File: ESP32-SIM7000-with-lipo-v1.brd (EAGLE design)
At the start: 90 x 60 mm, 65 parts, among them IC2 TXB0104, Q1 BSS138L, Q2 BSS138L, Q3 9013, Q5 9013, U3 ESP-WROOM-32, U4 MCP73831T-2ACI/OT, X1 LTE-uFL

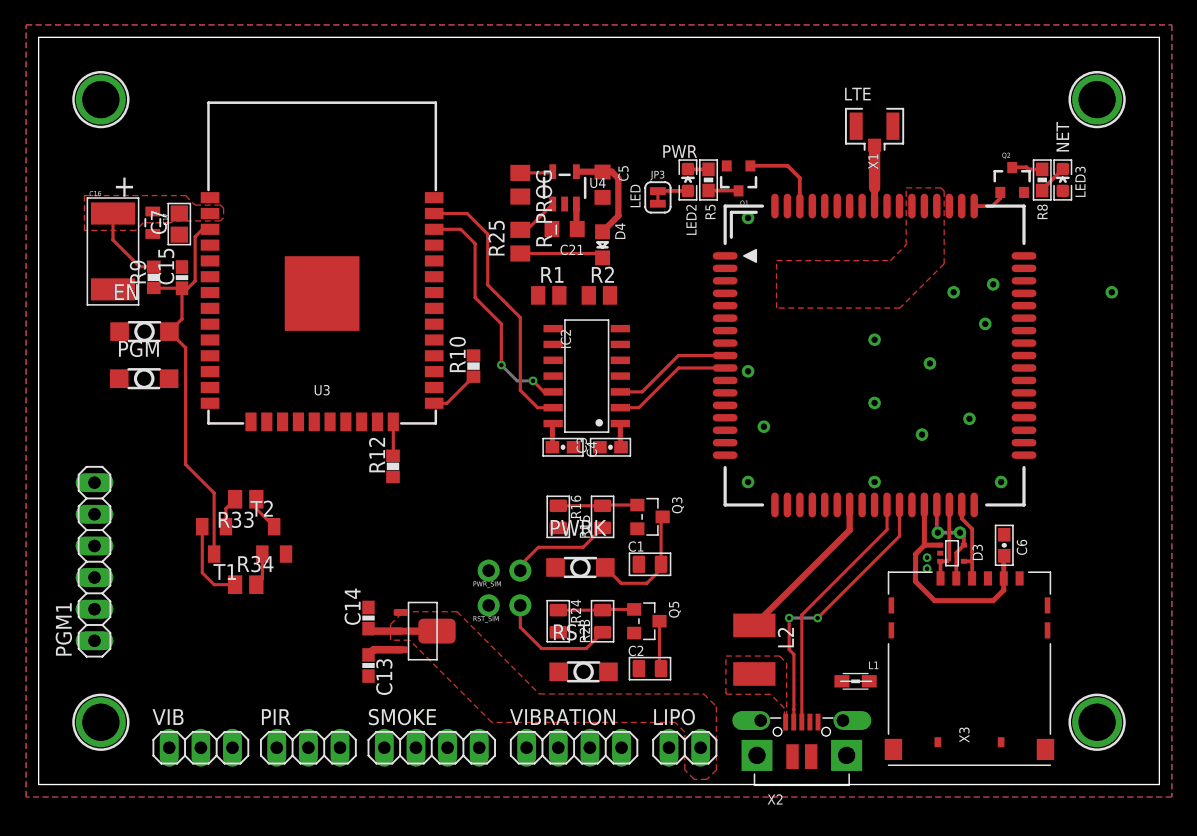
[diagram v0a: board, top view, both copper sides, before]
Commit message: route remaining traces
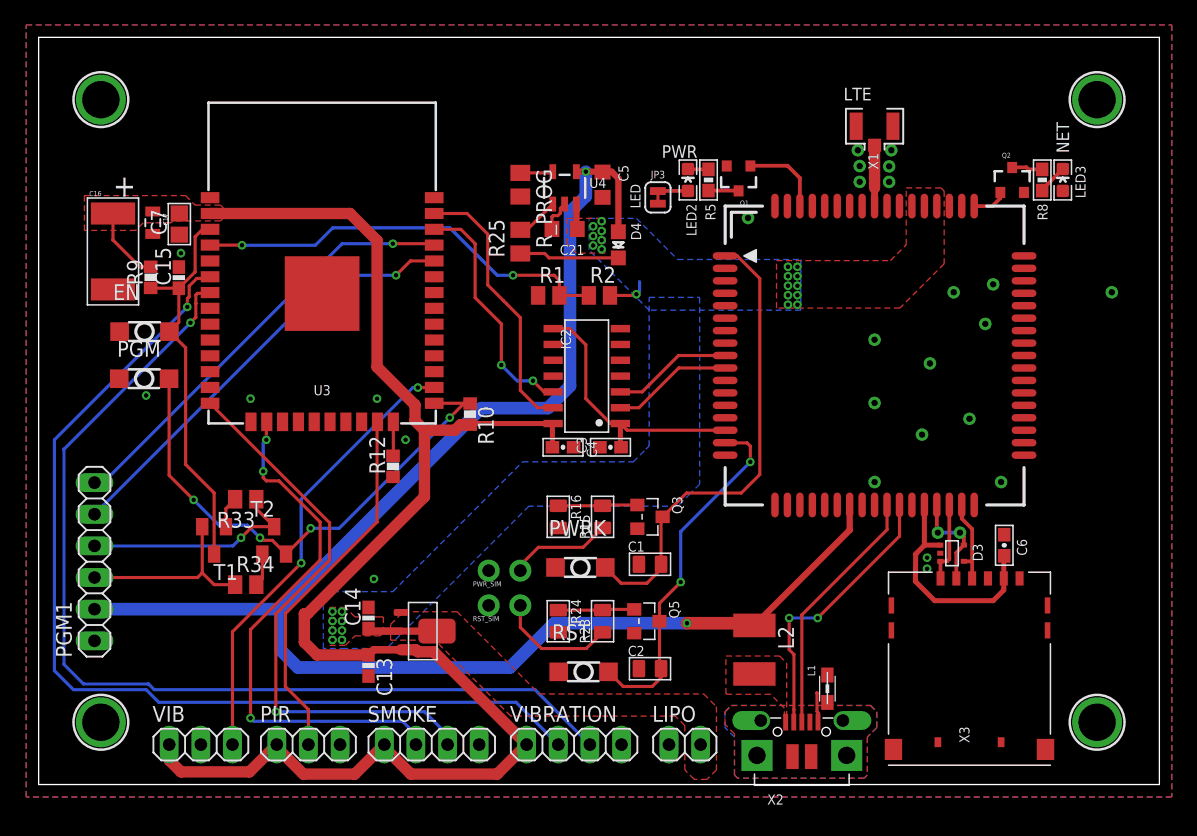
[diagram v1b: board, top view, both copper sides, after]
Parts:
- moved R10 3.86 mm to (34.6, 29.7), turned to 270 degrees
- moved L1 2.34 mm to (63.3, 7.69), turned to 270 degrees
- moved D4 1.27 mm to (46.6, 43.3)
- moved LIPO 0.25 mm to (51.9, 3.21)
- moved PIR 0.25 mm to (21.7, 3.21)
- moved SMOKE 0.25 mm to (31.6, 3.21)
- moved VIB 0.25 mm to (13.0, 3.21)
- moved VIBRATION 0.25 mm to (43.0, 3.21)
- moved C15 0.25 mm to (11.3, 40.7)
- moved R9 0.25 mm to (9.00, 40.7)
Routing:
- net +3V3: track 11.0 -> 127.9 mm
- net VBUS: track 21.3 -> 127.6 mm, vias 0 -> 2
- net VIB_SDA: track 0.00 -> 80.3 mm, vias 0 -> 1
- net VIB_SCL: track 0.00 -> 80.3 mm, vias 0 -> 1
- net SMOKE_SCL: track 0.00 -> 45.9 mm, vias 0 -> 1
- net SMOKE_SDA: track 0.00 -> 43.3 mm, vias 0 -> 3
- net IO0: track 4.04 -> 42.0 mm, vias 0 -> 4
- net VIBRATION: track 0.00 -> 36.4 mm, vias 0 -> 2
- net RXD0: track 0.00 -> 35.7 mm, vias 0 -> 1
- net TXD0: track 0.00 -> 35.3 mm, vias 0 -> 1
- net BAT_LEVEL: track 0.00 -> 33.9 mm, vias 0 -> 2
- net PIR: track 0.00 -> 29.8 mm
- net PWRKEY: track 9.72 -> 38.2 mm
- net SIM_RESET: track 3.86 -> 28.8 mm, vias 0 -> 2
- net 1.8V: track 1.93 -> 21.7 mm
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- added copper zone on layer 16, net +4.1V
- added copper zone on layer 1, net SHIELD
- added copper zone on layer 16, net SHIELD
- removed copper zone on layer 1, net N$3

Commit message: Naming components
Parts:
- renumbered PGM1 to PROGRAM

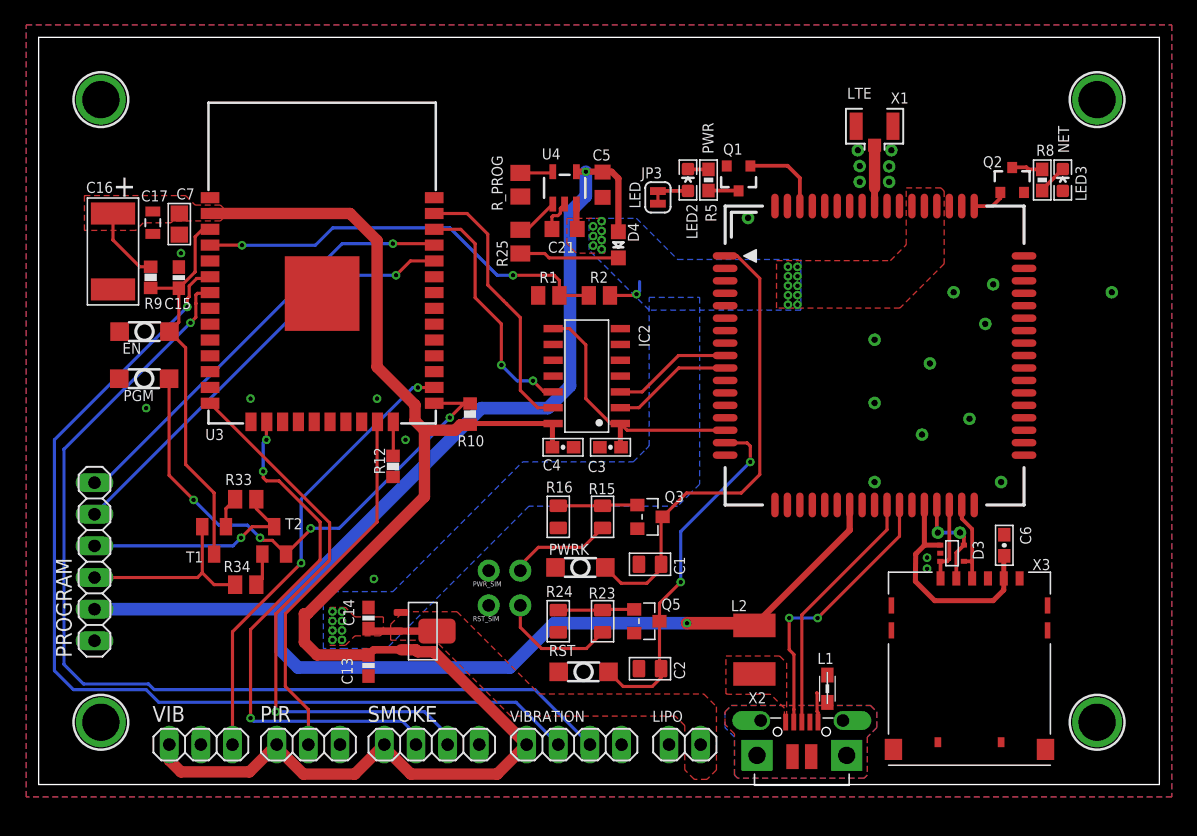
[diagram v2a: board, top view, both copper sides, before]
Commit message: adds vias and completes DRC
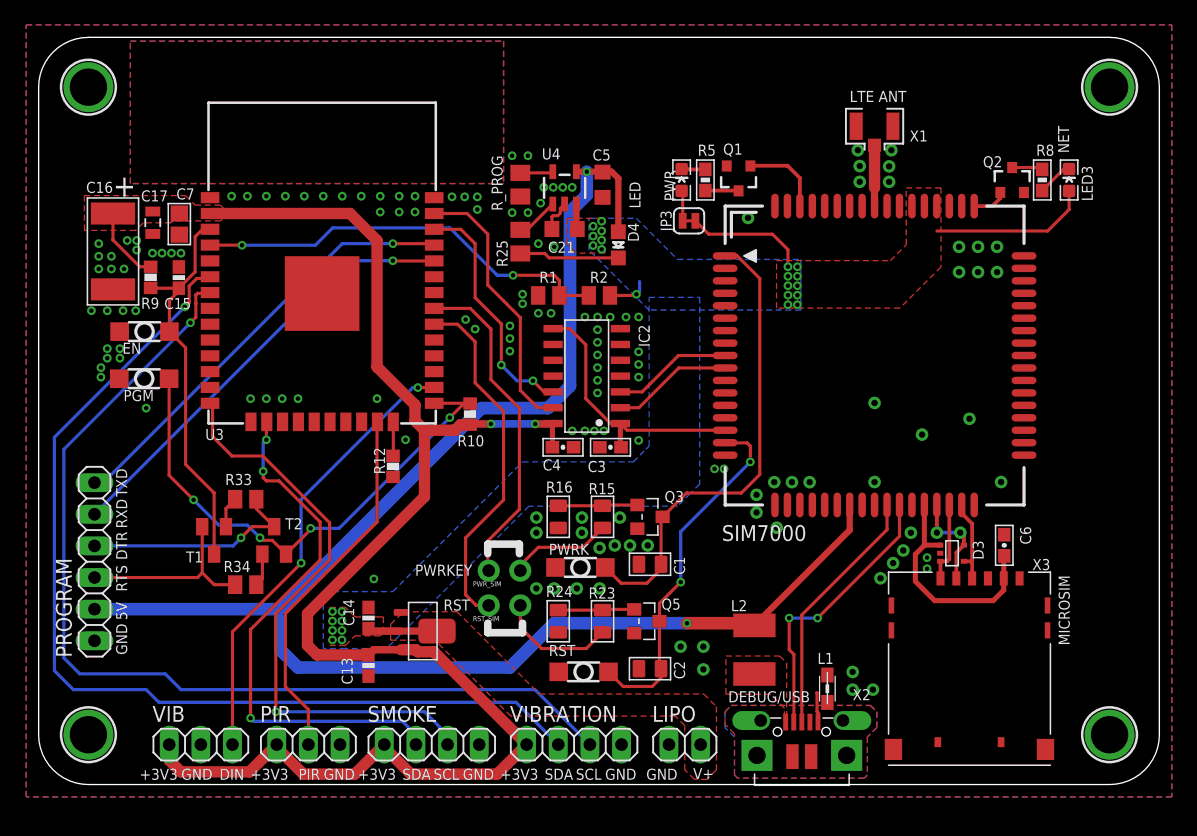
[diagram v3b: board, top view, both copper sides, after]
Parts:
- moved JP3 3.13 mm to (52.2, 45.3), turned to 180 degrees
- moved $H1 1.41 mm to (4.00, 4.00)
- moved $H2 1.41 mm to (86.0, 4.00)
- moved $H3 1.41 mm to (4.00, 56.0)
- moved $H4 1.41 mm to (86.0, 56.0)
- moved LED3 0.51 mm to (82.8, 48.5)
- moved LED2 0.51 mm to (51.6, 48.5)
- moved R5 0.25 mm to (53.5, 48.5)
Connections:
- removed net VIN: JP3.1, LED3.A
- net +4.1V: now also JP3.1, LED3.A
- net UC_PWRK: now also U3.31
- net UC_RST: now also U3.30
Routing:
- net UC_RST: track 0.00 -> 28.6 mm
- net UC_PWRK: track 0.00 -> 26.7 mm
- net +4.1V: track 8.00 -> 30.6 mm
- net SMOKE_SCL: track 45.9 -> 47.3 mm
- net N$11: track 2.41 -> 2.95 mm
- net +3V3: track 127.9 -> 127.6 mm, vias 0 -> 2
- net GND: vias 26 -> 139
- added copper zone on layer 1, net N$3
- added copper zone on layer 16, net N$6
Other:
- outline, holes or cut-outs redrawn
- board text added: "+3V3"
- board text added: "5V"
- board text added: "DEBUG/USB"
- board text added: "DIN"
- board text added: "DTR"
- board text added: "GND"
- board text added: "LTE ANT"
- board text added: "MICROSIM"
- board text added: "PIR"
- board text added: "PWRKEY"
- board text added: "RST"
- board text added: "RTS"
- board text added: "RXD"
- board text added: "SCL"
- board text added: "SDA"
- board text added: "SIM7000"
- board text added: "TXD"
- board text added: "V+"
- board text removed: "LTE"

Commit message: Schematic frames changes
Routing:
- net GND: vias 139 -> 142
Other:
- board text added: "ESP-WROOM-32"
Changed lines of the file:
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@@
 <drawing>
 <settings>
-<setting alwaysvectorfont="no"/>
+<setting alwaysvectorfont="yes"/>
 <setting verticaltext="up"/>
 </settings>
@@
 <board>
 <plain>
-<text x="82.751" y="50.706" size="0.889" layer="21" font="vector" rot="R90">NET</text>
-<text x="50.259" y="49.35" size="0.889" layer="21" font="vector" rot="R270">PWR</text>
+<text x="84.783" y="47.0484" size="0.889" layer="21" font="vector" rot="R90">NET</text>
+<text x="49.6494" y="49.35" size="0.889" layer="21" font="vector" rot="R270">PWR</text>
 <text x="69.69" y="55.7" size="0.889" layer="21" font="vector" rot="R180">LTE ANT</text>
 <text x="48.334" y="46.261" size="0.889" layer="21" font="vector" rot="R90">LED</text>
@@
 <wire x1="90" y1="56" x2="86" y2="60" width="0" layer="20" curve="90"/>
 <wire x1="4" y1="60" x2="0" y2="56" width="0" layer="20" curve="90"/>
+<text x="13.4112" y="26.416" size="1.27" layer="21" font="vector" ratio="10">ESP-WROOM-32</text>
 </plain>
 <attributes>
@@
 </element>
 <element name="LED3" library="TimWoo-LED" library_urn="urn:adsk.eagle:library:501982" package="LED-0603-MARKED" package3d_urn="urn:adsk.eagle:package:502010/2" value="Blue" x="82.751" y="48.547" smashed="yes" rot="R90">
-<attribute name="NAME" x="83.767" y="49.69" size="0.889" layer="25" font="vector" rot="R270"/>
 <attribute name="VALUE" x="84.148" y="47.531" size="0.4064" layer="27" rot="R90"/>
 </element>
@@
 <via x="45.0504" y="15.7464" extent="1-16" drill="0.508" diameter="1.016"/>
 <via x="39.9704" y="15.7464" extent="1-16" drill="0.508" diameter="1.016"/>
+<via x="73.914" y="39.116" extent="1-16" drill="0.508" diameter="1.016"/>
+<via x="75.5396" y="39.116" extent="1-16" drill="0.508" diameter="1.016"/>
+<via x="76.962" y="39.116" extent="1-16" drill="0.508" diameter="1.016"/>
 </signal>
 <signal name="1.8V">

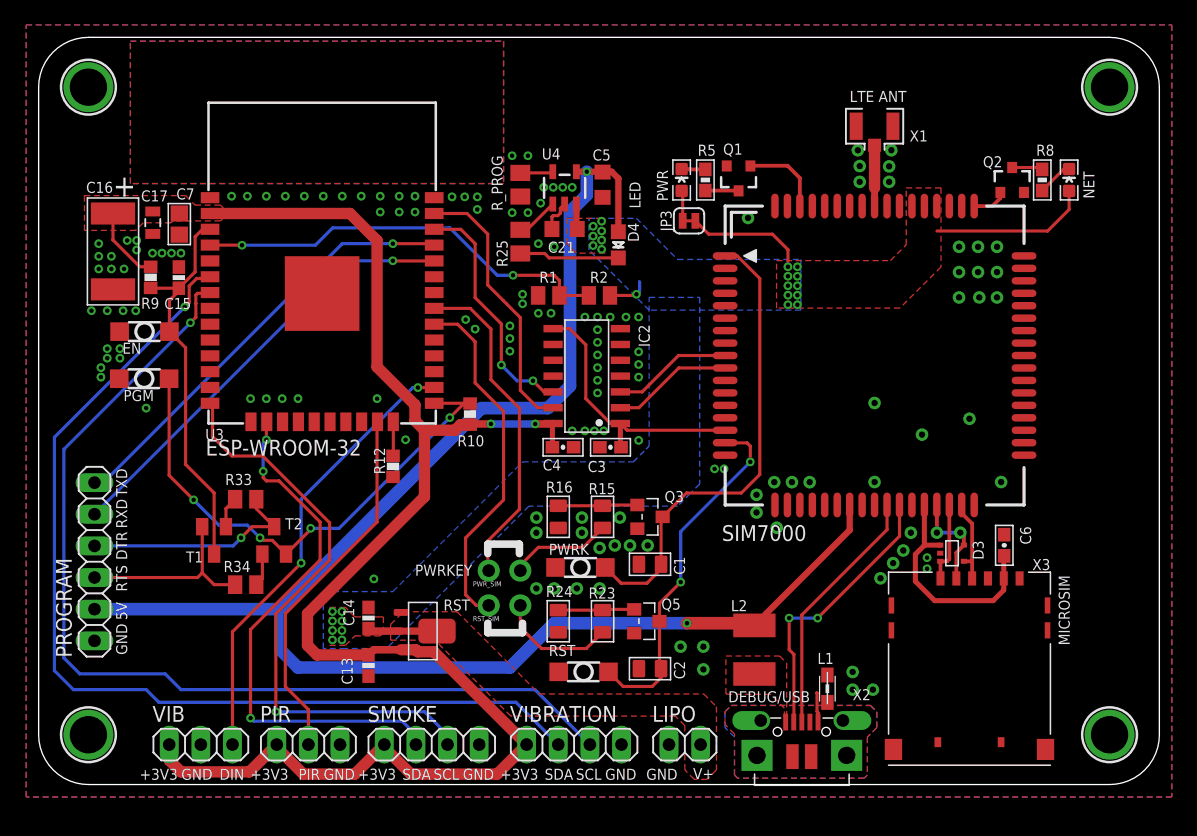
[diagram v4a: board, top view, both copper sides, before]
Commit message: Logo and config switch
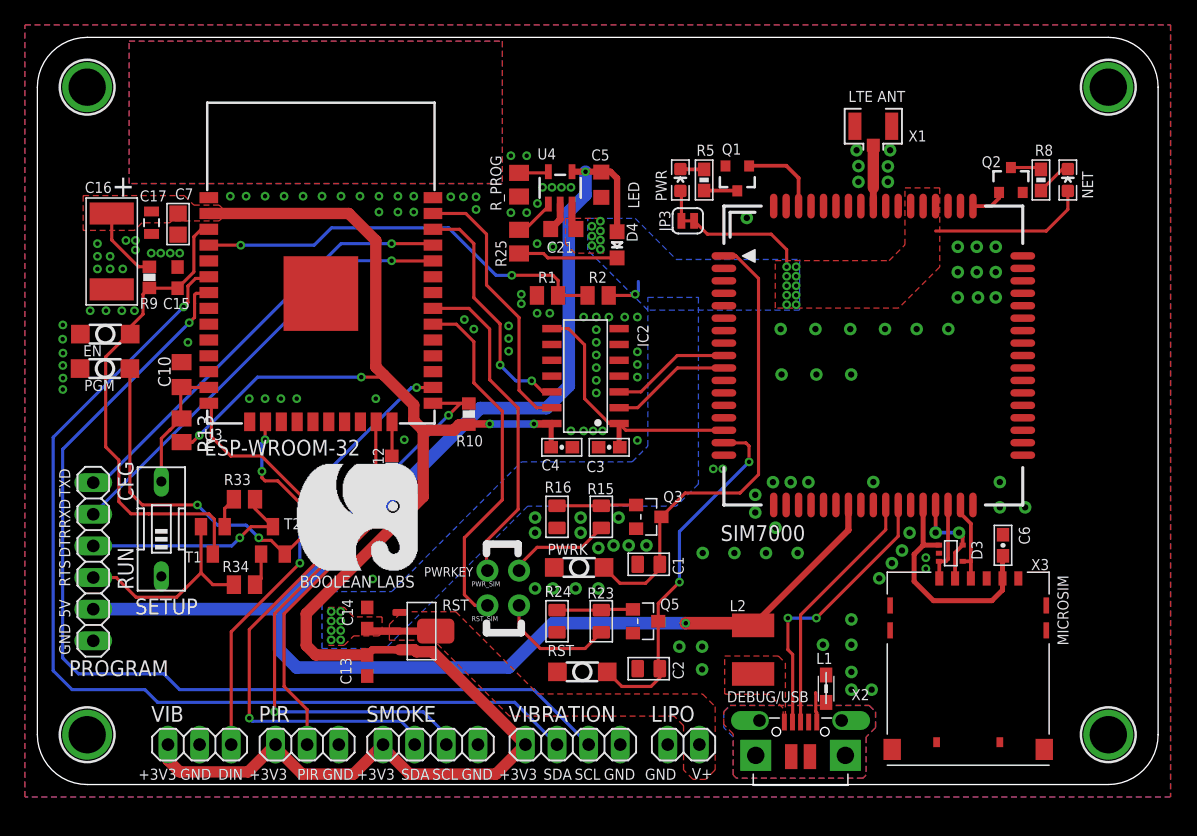
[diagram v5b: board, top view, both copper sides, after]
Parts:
- added C10: 0.1uF/16V, rcl:C0805K
- added R13: 12k, rcl:M0805
- added SETUP: (no value), special:EDG-01
- R10, R12, R9: device rcl:R0603 -> rcl:R0603@1
- moved PGM 3.25 mm to (5.33, 33.4)
- moved EN 3.16 mm to (5.35, 36.2)
- moved U4 0.36 mm to (41.9, 47.9)
- moved $H2 0.10 mm to (85.9, 4.00)
- moved $H4 0.10 mm to (85.9, 56.0)
- moved C5 0.10 mm to (45.2, 48.2)
- moved L1 0.10 mm to (63.2, 7.69)
- moved L2 0.10 mm to (57.4, 10.8)
- moved LED2 0.10 mm to (51.5, 48.5)
- moved LED3 0.10 mm to (82.6, 48.5)
- moved PWRK 0.10 mm to (43.4, 17.4)
- moved Q2 0.10 mm to (78.1, 48.5)
- moved R1 0.10 mm to (40.9, 39.3)
- moved R10 0.10 mm to (34.5, 29.7)
- moved R15 0.10 mm to (45.2, 21.5)
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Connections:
- new net CONFIG: C10.1, R13.1, SETUP.2, U3.13
- net +3V3: now also R13.2
- net GND: now also C10.2, SETUP.1
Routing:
- net +3V3: track 127.6 -> 146.1 mm, vias 2 -> 4
- net CONFIG: track 0.00 -> 10.6 mm
- net EN: track 31.5 -> 38.6 mm
- net IO0: track 42.0 -> 47.2 mm
- net RTS: track 15.6 -> 16.9 mm
- net GND: track 5.05 -> 4.71 mm, vias 142 -> 157
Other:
- board text added: "BOOLEAN LABS"
- board text added: "CFG"
- board text added: "RUN"

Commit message: Adds TVS and small caps to Vbat pins
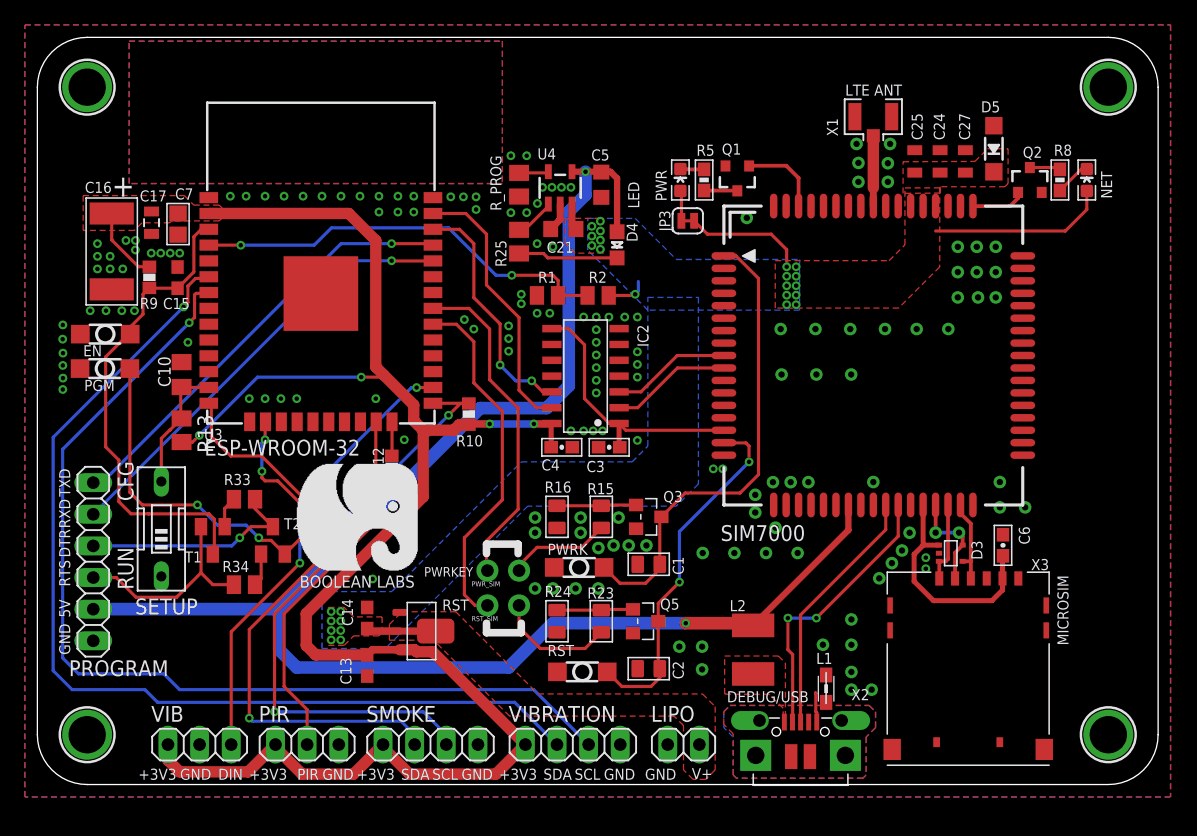
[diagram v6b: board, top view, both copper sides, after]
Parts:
- added C24: 22uF, SparkFun-Capacitors:0805
- added C25: 33pF, SparkFun-Capacitors:0805
- added C27: 10pF, SparkFun-Capacitors:0805
- added D5: MMSZ5231BT1G, Adafruit SIM808 Breakout:SOD-123
- moved LED3 1.52 mm to (84.2, 48.5)
- moved Q2 1.52 mm to (79.6, 48.5)
- moved R8 1.52 mm to (82.0, 48.5)
- moved X1 0.76 mm to (67.0, 53.6)
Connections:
- removed net LTE_DTR: U1.3
- removed net LTE_RI: U1.4
- removed net UC_DTR: IC2.10
- removed net UC_RI: IC2.11
- net +4.1V: now also C24.1, C25.1, C27.1, D5.C
- net GND: now also C24.2, C25.2, C27.2, D5.A
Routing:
- net NETLIGHT: track 2.82 -> 4.35 mm
- net +4.1V: track 30.7 -> 32.2 mm
- net RF_ANT: track 4.89 -> 5.65 mm
